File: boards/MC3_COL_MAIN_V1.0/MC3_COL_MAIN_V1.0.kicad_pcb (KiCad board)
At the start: 4 copper layers, 66 x 66 mm, 107 parts, among them J1 SUPPLY_IN, J10 MOTOR, J11 MOTOR, J12 CAN, J2 SWD, J3 ENC_leaf1, J4 ENC_leaf2, J5 ENC_leaf3, J6 ENC_leaf4, J7 MOTOR, J8 MOTOR, J9 MOTOR, Q1 AO4407C, SW1 SKRKAEE020, U1 AMS1117-3.3, U2 STM32F412RET6, U3 DRV8214RTER, U4 DRV8214RTER, U5 DRV8214RTER, U6 DRV8214RTER, U7 DRV8214RTER, U8 TJA1051T/3, Y1 8MHz

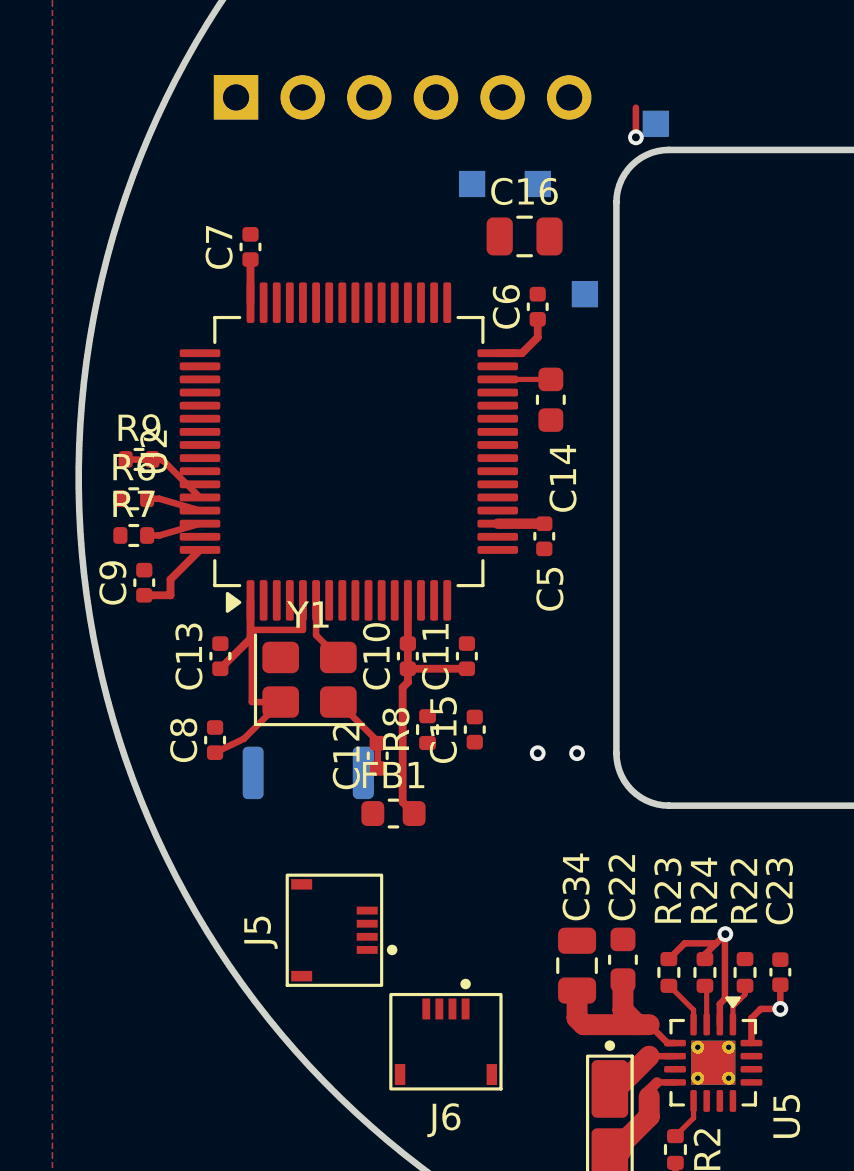
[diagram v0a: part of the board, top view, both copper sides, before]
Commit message: PCB: nFAULT_leaf3 routed MCU-to-driver as the fan-out example; I2C bus decision
nFAULT_leaf3 is now complete end to end - U5.4, R23.2 and U2.10 all connected -
as the worked example of how a channel signal reaches the MCU:

  F.Cu straight out of the pin row, north through the 0.7 mm gap between the two
  pull-ups at x 90.19, via down at (90.19, 117.0), B.Cu west along the empty
  corridor to (78.05, 107.5), via up, F.Cu straight into pin 10.

Both escapes leave their pin row straight before turning. A diagonal off a
0.5 mm pin crosses its neighbours - that is what shorted OSC_IN to pin 3 and
OSC_OUT to pin 7 earlier.

The fan-out via sits inside the leaf3 rule area and the B.Cu haul outside it, so
Repeat Layout copies the escape to every channel but not the run to the MCU,
which differs per channel.

MIGRATION section 9 records the I2C decision: stay on one bus. Estimated bus
capacitance is ~70 pF against the 400 pF limit, which closes the vault's open
item, and 4.7k gives ~280 ns rise against Fast-mode's 300 ns - inside but tight,
so 2.2k is worth considering. Bandwidth, addressing, firmware and layout all
favour one bus; the cost is that one stuck device takes out all five channels.

Co-Authored-By: Claude Opus 5 (1M context) <noreply@anthropic.com>
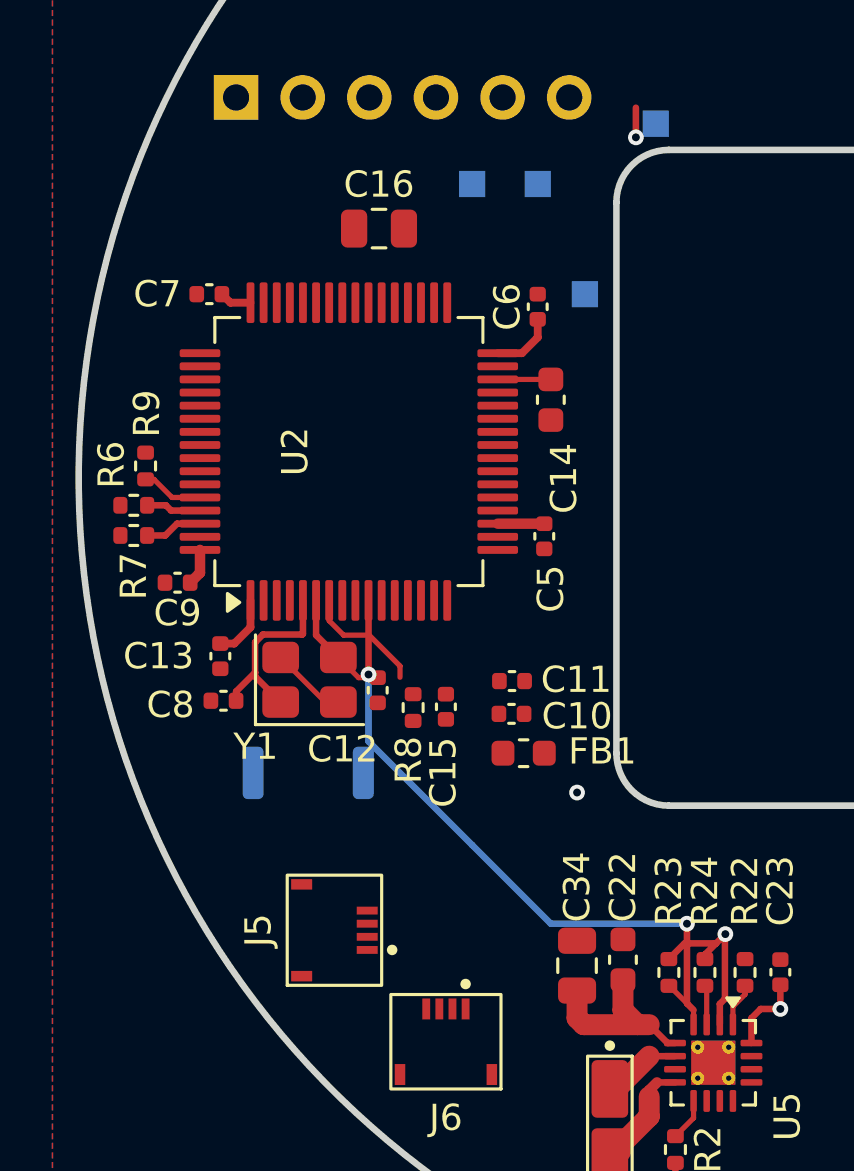
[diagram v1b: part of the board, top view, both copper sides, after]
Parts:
- moved C16 5.56 mm to (78.5, 90.5)
- moved FB1 5.47 mm to (84.0, 110.5), turned to 180 degrees
- moved C10 4.52 mm to (83.5, 109.0), turned to 0 degrees
- moved C12 2.50 mm to (78.4, 108.1), turned to -90 degrees
- moved C7 2.39 mm to (72.0, 93.0), turned to 180 degrees
- moved C11 1.96 mm to (83.5, 107.8), turned to 0 degrees
- moved C8 1.53 mm to (72.5, 108.5), turned to 180 degrees
- moved C15 1.40 mm to (81.0, 108.7), turned to -90 degrees
- moved C9 1.27 mm to (70.8, 104.0), turned to 180 degrees
- moved R8 1.00 mm to (79.8, 108.8)
- moved R9 0.35 mm to (69.5, 99.5), turned to 90 degrees
- moved R6 0.25 mm to (69.1, 101.0)
- turned C13 to -90 degrees
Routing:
- net nFAULT_leaf3: track 1.88 -> 25.7 mm, vias 0 -> 2
- net /MCU/VDDA: track 10.6 -> 0.00 mm
- net /MCU/NRST: track 0.00 -> 4.62 mm
- net +3V3: track 66.4 -> 63.6 mm
- net /MCU/OSC_IN: track 10.1 -> 7.29 mm
- net /MCU/BOOT0: track 3.43 -> 2.36 mm
- net GND: track 6.51 -> 7.33 mm, vias 4 -> 3
- net /MCU/OSC_OUT: track 3.56 -> 4.35 mm

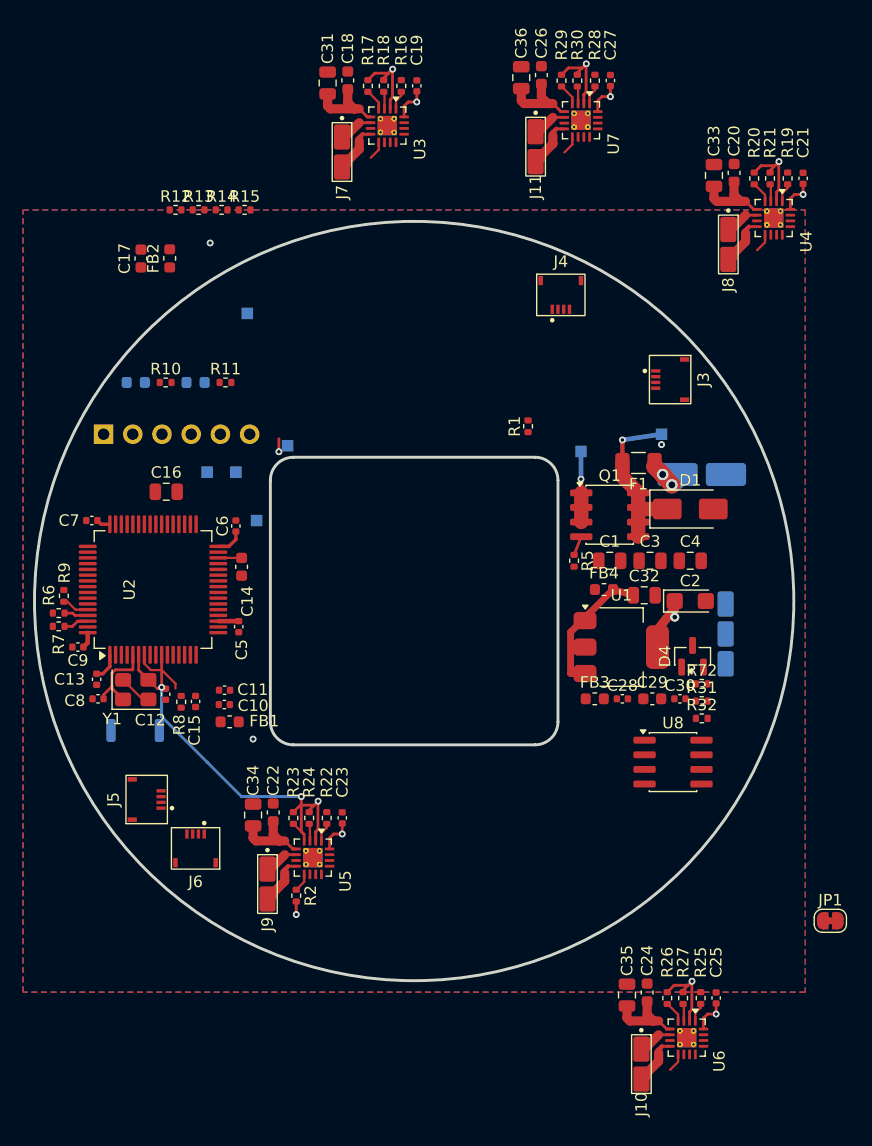
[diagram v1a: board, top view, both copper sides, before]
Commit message: WIP before MCU pin remap: board state, vault sync, GND vias placed
Co-Authored-By: Claude Fable 5 <noreply@anthropic.com>
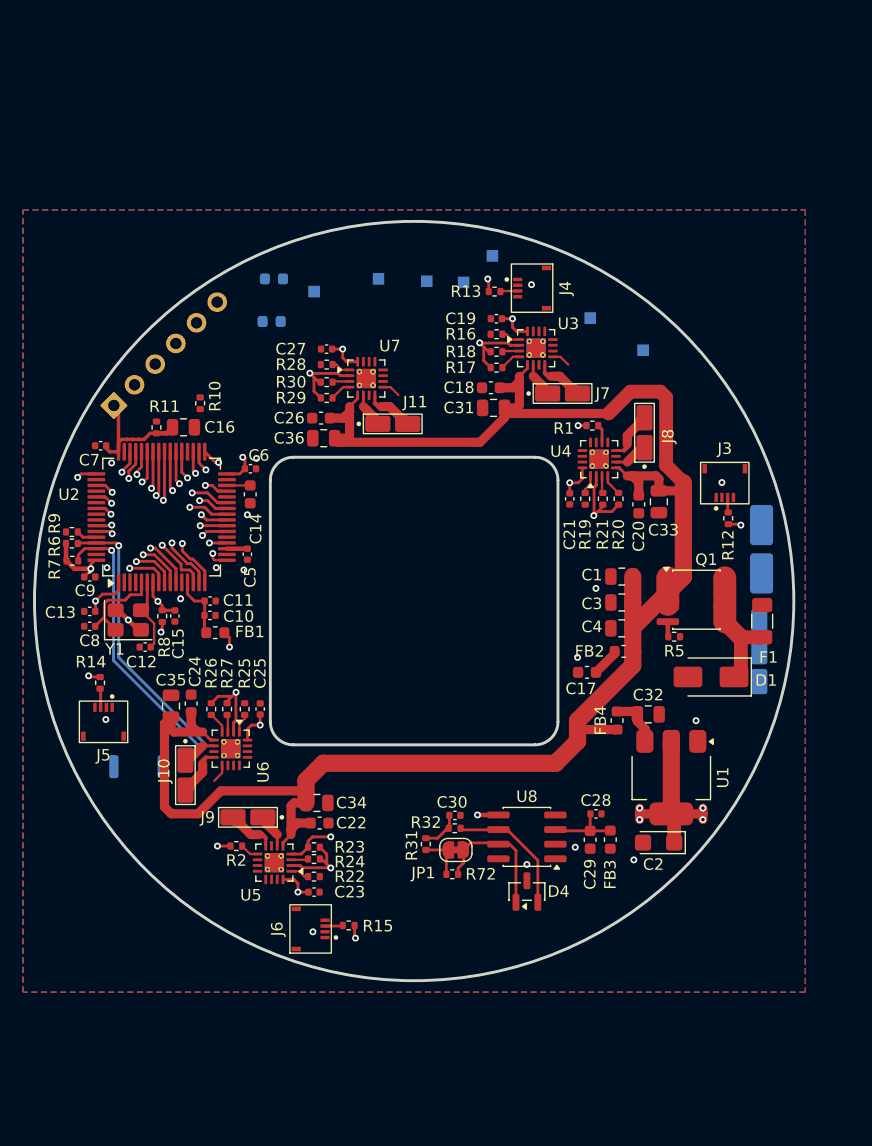
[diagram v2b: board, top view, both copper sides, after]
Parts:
- moved R15 62.9 mm to (94.3, 128.2), turned to 180 degrees
- moved R12 55.0 mm to (127.3, 92.8), turned to 90 degrees
- moved C17 52.9 mm to (115.0, 106.2), turned to 180 degrees
- moved FB2 52.2 mm to (118.2, 104.4), turned to 180 degrees
- moved C24 46.9 mm to (80.6, 108.9)
- moved C25 46.9 mm to (86.6, 109.4)
- moved C35 46.9 mm to (78.9, 109.1)
- moved J10 46.9 mm to (80.1, 115.1)
- moved R26 46.9 mm to (82.4, 109.4)
- moved R27 46.9 mm to (83.7, 109.4)
- moved R25 46.9 mm to (85.3, 109.4)
- moved U6 46.9 mm to (84.1, 112.8)
- moved R14 42.4 mm to (72.7, 107.1), turned to -90 degrees
- moved C36 35.7 mm to (92.1, 85.8), turned to 180 degrees
- moved C26 35.4 mm to (91.9, 84.1), turned to 180 degrees
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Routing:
- net VM: track 41.7 -> 162.4 mm, vias 1 -> 0
- net +3V3: track 63.6 -> 102.8 mm, vias 12 -> 26
- net I2C1_SDA: track 2.20 -> 24.3 mm, vias 0 -> 1
- net I2C1_SCL: track 2.10 -> 24.1 mm, vias 0 -> 1
- net nFAULT_leaf3: track 25.7 -> 8.32 mm
- net /CAN/CANH: track 0.00 -> 11.9 mm
- net /CAN/CANL: track 0.00 -> 11.5 mm
- net /Power/VM_LDO: track 11.9 -> 4.53 mm
- net ENC_leaf3: track 0.00 -> 6.43 mm, vias 0 -> 1
- net /CAN/VCAN5: track 0.00 -> 6.31 mm
- net ENC_leaf4: track 0.00 -> 6.14 mm, vias 0 -> 1
- net /MCU/VDDA: track 0.00 -> 5.59 mm
- net ENC_leaf2: track 0.00 -> 5.42 mm, vias 0 -> 1
- net /Power/VIN_PAD: track 4.43 -> 0.00 mm, vias 2 -> 0
- net IPROPI_leaf3: track 1.67 -> 5.97 mm, vias 0 -> 1
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
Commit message: PCB fully routed: 0 unconnected, 0 clearance errors
MCU remap landed (channels grouped by edge), I2C/nSLEEP bus on In2 with F.Cu
jump-overs, VSENS arc on B.Cu, CAN chain J12->D4->termination->U8, GND islands
resolved (5 vias + 3 stubs), VIN_PAD feed rebuilt at 2.0mm with 2x 1.0/0.6 vias.
Remaining known items: min-through-hole constraint to restore to 0.2 (20 false
drill errors), 3 dangling via stubs, footprint library re-sync deferred to
pre-fab silk pass.

Co-Authored-By: Claude Fable 5 <noreply@anthropic.com>
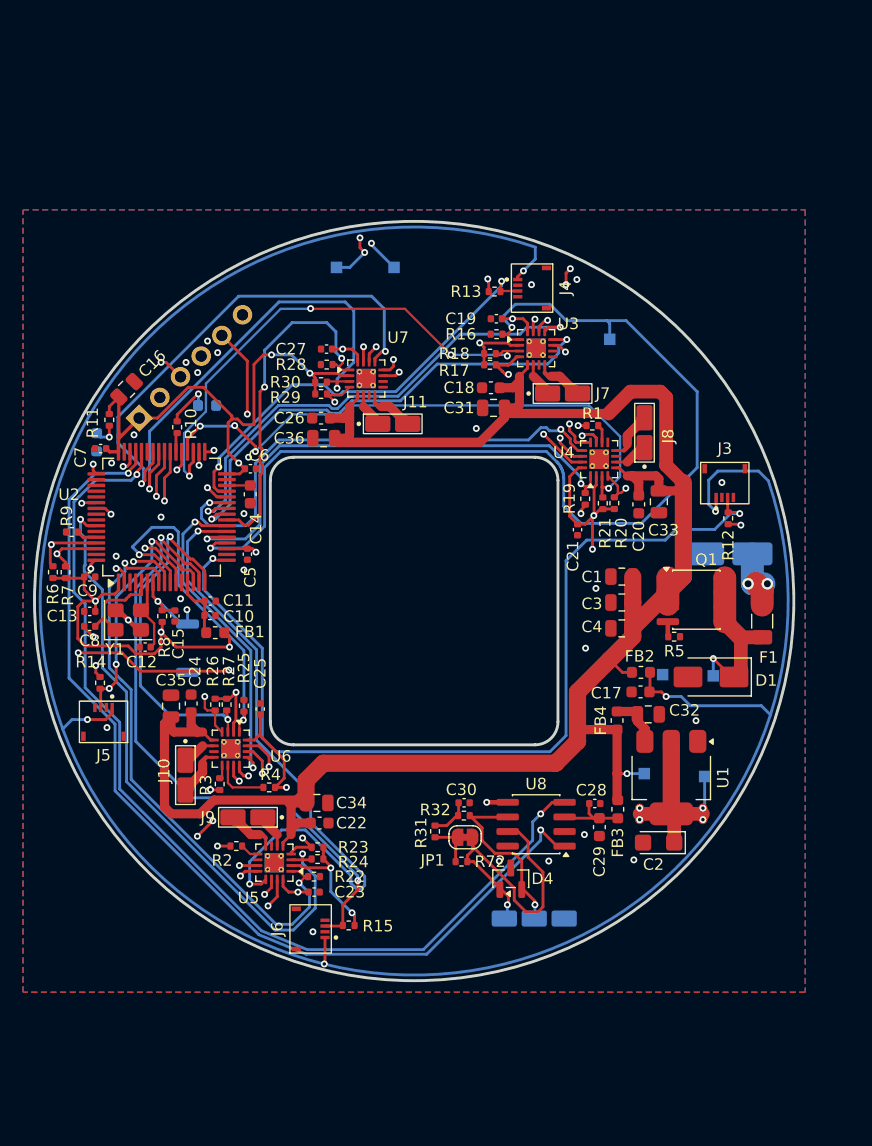
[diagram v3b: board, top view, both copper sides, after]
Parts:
- added R3: 2.2k, MC3_COL_MAIN:R_0402_1005Metric, F.Cu at (83.1, 115.9)
- added R4: 2.2k, MC3_COL_MAIN:R_0402_1005Metric, F.Cu at (87.4, 116.2)
- moved TP3 51.7 mm to (125.2, 115.2)
- moved TP1 46.9 mm to (120.0, 115.0)
- moved TP2 32.9 mm to (126.0, 106.5)
- moved J12 30.3 mm to (110.4, 127.6), turned to 0 degrees
- moved TP7 28.3 mm to (121.6, 106.4)
- moved TP6 26.0 mm to (117.0, 77.2)
- moved D3 21.0 mm to (72.4, 86.2), turned to 90 degrees
- moved SW1 11.2 mm to (80.3, 104.1), turned to -90 degrees
- moved TP4 11.1 mm to (93.2, 71.0)
- moved D2 9.21 mm to (82.0, 83.0), turned to 180 degrees
- moved C16 5.95 mm to (75.0, 81.6), turned to 45 degrees
- moved C17 4.95 mm to (119.7, 107.9)
- moved R11 4.15 mm to (73.5, 84.2), turned to -90 degrees
- moved TP5 3.09 mm to (98.2, 71.0)
- moved R6 2.99 mm to (68.6, 97.5), turned to 90 degrees
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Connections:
- U2 pad 10: nFAULT_leaf3 -> IPROPI_leaf4
- U2 pad 11: PH_leaf3 -> nFAULT_leaf4
- U2 pad 16: IPROPI_leaf3 -> RC_OUT_leaf4
- U2 pad 17: PH_leaf4 -> ENC_leaf1
- U2 pad 2: unconnected-(U2-PC13-Pad2) -> PH_leaf3
- U2 pad 20: IPROPI_leaf4 -> IPROPI_leaf1
- U2 pad 21: /MCU/LED_HB -> IPROPI_leaf2
- U2 pad 25: DRV_nSLEEP -> PH_leaf1
- U2 pad 26: IPROPI_leaf2 -> EN_leaf1
- U2 pad 27: IPROPI_leaf1 -> EN_leaf2
- U2 pad 28: unconnected-(U2-PB2/BOOT1-Pad28) -> nFAULT_leaf1
- U2 pad 29: ENC_leaf1 -> ENC_leaf2
- U2 pad 33: PH_yaw -> PH_leaf2
- U2 pad 34: RC_OUT_yaw -> nFAULT_leaf2
- U2 pad 35: RC_OUT_leaf4 -> RC_OUT_leaf1
- U2 pad 36: unconnected-(U2-PB15-Pad36) -> RC_OUT_leaf2
- U2 pad 37: PH_leaf2 -> DRV_nSLEEP
- U2 pad 38: PH_leaf1 -> /MCU/LED_HB
- U2 pad 39: EN_leaf2 -> nFAULT_yaw
- U2 pad 40: EN_leaf1 -> PH_yaw
- U2 pad 41: ENC_leaf2 -> RC_OUT_yaw
- U2 pad 43: RC_OUT_leaf3 -> unconnected-(U2-PA10-Pad43)
- U2 pad 51: nFAULT_leaf4 -> unconnected-(U2-PC10-Pad51)
- U2 pad 53: nFAULT_yaw -> unconnected-(U2-PC12-Pad53)
- U2 pad 54: unconnected-(U2-PD2-Pad54) -> PH_leaf4
- U2 pad 58: RC_OUT_leaf1 -> RC_OUT_leaf3
- U2 pad 59: RC_OUT_leaf2 -> unconnected-(U2-PB7-Pad59)
- U2 pad 8: nFAULT_leaf1 -> IPROPI_leaf3
- U2 pad 9: nFAULT_leaf2 -> nFAULT_leaf3
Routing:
- net DRV_nSLEEP: track 3.47 -> 136.7 mm, vias 1 -> 8
- net +3V3: track 102.8 -> 194.9 mm, vias 26 -> 29
- net IPROPI_leaf1: track 5.04 -> 89.5 mm, vias 1 -> 2
- net CAN1_RX: track 2.14 -> 85.6 mm, vias 1 -> 2
- net CAN1_TX: track 2.57 -> 85.4 mm, vias 1 -> 2
- net ENC_leaf1: track 3.40 -> 81.2 mm, vias 1 -> 2
- net PH_leaf4: track 1.72 -> 68.7 mm, vias 1 -> 4
- net I2C1_SCL: track 24.1 -> 89.2 mm, vias 1 -> 10
- net nFAULT_leaf2: track 5.63 -> 66.3 mm, vias 1 -> 2
- net I2C1_SDA: track 24.3 -> 82.7 mm, vias 1 -> 8
- net EN_leaf3: track 2.27 -> 57.3 mm, vias 1 -> 2
- net RC_OUT_leaf3: track 4.37 -> 56.2 mm, vias 1 -> 2
- net nFAULT_leaf3: track 8.32 -> 58.2 mm
- net ENC_leaf4: track 6.14 -> 54.7 mm, vias 1 -> 2
- net RC_OUT_leaf2: track 2.96 -> 50.8 mm, vias 1 -> 4
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
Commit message: Homing interrupter -> GP1S094HCZ0F (C920601, 3mm slot, user decision); COL-COTS-0034, 0033 rejected
Co-Authored-By: Claude Fable 5 <noreply@anthropic.com>
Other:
- rule pad_to_mask_clearance: 0.05 -> 0
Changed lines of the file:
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@@
 			(dielectric_constraints no)
 		)
-		(pad_to_mask_clearance 0.05)
+		(pad_to_mask_clearance 0)
 		(allow_soldermask_bridges_in_footprints no)
 		(tenting
@@
 		(grid_origin 100 100)
 		(pcbplotparams
-			(layerselection 0x00000000_00000000_55555555_5755f5ff)
+			(layerselection 0x00000000_00000000_55555555_575555ff)
 			(plot_on_all_layers_selection 0x00000000_00000000_00000000_00000000)
 			(disableapertmacros no)
-			(usegerberextensions no)
+			(usegerberextensions yes)
 			(usegerberattributes yes)
 			(usegerberadvancedattributes yes)
@@
 			(sketchdnponfab yes)
 			(crossoutdnponfab yes)
-			(subtractmaskfromsilk no)
+			(subtractmaskfromsilk yes)
 			(outputformat 1)
 			(mirror no)
-			(drillshape 1)
+			(drillshape 0)
 			(scaleselection 1)
-			(outputdirectory "")
+			(outputdirectory "fab/")
 		)
 	)
@@
 		(tags "capacitor")
 		(property "Reference" "C35"
-			(at 2.256273 0 0)
+			(at 2.256273 -0.116001 0)
 			(layer "F.SilkS")
 			(effects
@@
 		(tags "capacitor")
 		(property "Reference" "C20"
-			(at 2.775 0 90)
+			(at 2.903772 0 90)
 			(layer "F.SilkS")
 			(effects
@@
 		(tags "resistor")
 		(property "Reference" "R12"
-			(at -2.34 0 90)
+			(at -1.69 -0.8 180)
 			(layer "F.SilkS")
 			(effects
@@
 		(tags "resistor")
 		(property "Reference" "R26"
-			(at -2.9 0.2 90)
+			(at -2.9 0.429185 90)
 			(layer "F.SilkS")
 			(effects
@@
 		(tags "WQFN NoLead Texas_RTE0016C")
 		(property "Reference" "U3"
-			(at 2.798772 -2.12 0)
+			(at 3.648772 -1.77 0)
 			(layer "F.SilkS")
 			(effects
@@
 		(descr "Panasonic AYF530435 (Y5B series) 0.5 mm pitch 4-position FFC/FPC connector, right-angle SMD, back-lock, 1.00 mm mounted height. LCSC C425129. Land pattern from the JLCPCB/EasyEDA footprint of C425129 (4 signal pads 0.3x0.8 on 0.5 mm, two 0.4x0.8 mechanical pads at +/-1.75). Vault: Main-Board-01 Connectors, Encoder Connectors.")
 		(property "Reference" "J4"
-			(at 0 -2.9 90)
+			(at 1.2 -2.9 180)
 			(layer "F.SilkS")
 			(effects
@@
 		(tags "capacitor")
 		(property "Reference" "C33"
-			(at 2.469251 -0.401001 0)
+			(at 3.128772 0.021499 90)
 			(layer "F.SilkS")
 			(effects
@@
 		(tags "capacitor")
 		(property "Reference" "C6"
-			(at 0.73 -1.16 0)
+			(at -0.77 -1.75 0)
 			(layer "F.SilkS")
 			(effects
@@
 		(tags "resistor")
 		(property "Reference" "R72"
-			(at -2.49 0 0)
+			(at -0.14 -1.35 0)
 			(layer "F.SilkS")
 			(effects
@@
 		(tags "capacitor")
 		(property "Reference" "C5"
-			(at 2 -0.25 90)
+			(at 2 -0.75 90)
 			(layer "F.SilkS")
 			(effects
@@
 		(tags "solder pad motor termination bare copper")
 		(property "Reference" "J7"
-			(at 3.5 0 0)
+			(at 3.6 0 0)
 			(layer "F.SilkS")
 			(effects
@@
 		(tags "capacitor")
 		(property "Reference" "C8"
-			(at 0 -1.25 0)
+			(at 2.3 -0.55 0)
 			(layer "F.SilkS")
 			(effects
@@
 		(tags "capacitor")
 		(property "Reference" "C23"
-			(at 3.098886 0 0)
+			(at 2.328795 0.201228 0)
 			(layer "F.SilkS")
 			(effects
@@
 		(tags "capacitor")
 		(property "Reference" "C13"
-			(at 2.4 -0.4 0)
+			(at 2.8 -0.4 0)
 			(layer "F.SilkS")
 			(effects
@@
 		(tags "resistor")
 		(property "Reference" "R25"
-			(at 3.292387 0 90)
+			(at 2.984974 -0.139723 90)
 			(layer "F.SilkS")
 			(effects
@@
 		(tags "resistor")
 		(property "Reference" "R22"
-			(at 3.108886 0 0)
+			(at 2.3088 0.297925 0)
 			(layer "F.SilkS")
 			(effects
@@
 		(tags "resistor")
 		(property "Reference" "R27"
-			(at -2.9 -0.2 90)
+			(at -2.446309 0.124437 90)
 			(layer "F.SilkS")
 			(effects
@@
 		(tags "resistor")
 		(property "Reference" "R14"
-			(at -1.81 0.8 180)
+			(at 0.14 1.95 180)
 			(layer "F.SilkS")
 			(effects
@@
 		(tags "capacitor")
 		(property "Reference" "C25"
-			(at 3.098886 0 90)
+			(at 2.603739 -0.127249 90)
 			(layer "F.SilkS")
 			(effects
